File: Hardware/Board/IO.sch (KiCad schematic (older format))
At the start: 45 parts, among them U3 TJA1029T, U4 TJA1029T, U5 TJA1029T, U6 TJA1049T-3, U7 MAX3072E

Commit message: Board to Board Verbindung eingefügt
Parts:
- added C64: 100nF, Capacitor_SMD:C_0603_1608Metric, symbol Device:C
- added U2: PCF8574A, symbol Interface_Expansion:PCF8574A
- gave numbers to parts that had none: 4
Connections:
- wire segments 158 -> 178
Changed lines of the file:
@@
 EESchema Schematic File Version 4
 LIBS:Womo-cache
-EELAYER 29 0
+EELAYER 26 0
 EELAYER END
 $Descr A3 16535 11693
@@
 I2C2_SCL
 $Comp
-L Interface_Expansion:PCF8574A U?
+L Interface_Expansion:PCF8574A U1
 U 1 1 5CF888F7
 P 7200 6600
-F 0 "U?" H 6750 7350 50  0000 C CNN
+F 0 "U1" H 6750 7350 50  0000 C CNN
 F 1 "PCF8574A" H 6850 7250 50  0000 C CNN
 F 2 "" H 7200 6600 50  0001 C CNN
@@
 	7700 6200 7850 6200
 $Comp
-L power:GND #PWR?
+L power:GND #PWR0126
 U 1 1 5CFC8198
 P 6350 6750
-F 0 "#PWR?" H 6350 6500 50  0001 C CNN
+F 0 "#PWR0126" H 6350 6500 50  0001 C CNN
 F 1 "GND" H 6355 6577 50  0000 C CNN
 F 2 "" H 6350 6750 50  0001 C CNN
@@
 	6350 6700 6350 6750
 $Comp
-L power:+3.3V #PWR?
+L power:+3.3V #PWR0134
 U 1 1 5CFDD90C
 P 7200 5650
-F 0 "#PWR?" H 7200 5500 50  0001 C CNN
+F 0 "#PWR0134" H 7200 5500 50  0001 C CNN
 F 1 "+3.3V" H 7215 5823 50  0000 C CNN
 F 2 "" H 7200 5650 50  0001 C CNN
@@
 $EndComp
 $Comp
-L Device:C C?
+L Device:C C14
 U 1 1 5CFE3BF0
 P 7450 5750
-F 0 "C?" V 7198 5750 50  0000 C CNN
+F 0 "C14" V 7198 5750 50  0000 C CNN
 F 1 "100nF" V 7289 5750 50  0000 C CNN
 F 2 "Capacitor_SMD:C_0603_1608Metric" H 7488 5600 50  0001 C CNN
@@
 $EndComp
 $Comp
-L power:GND #PWR?
+L power:GND #PWR0140
 U 1 1 5CFE91D8
 P 7900 5800
-F 0 "#PWR?" H 7900 5550 50  0001 C CNN
+F 0 "#PWR0140" H 7900 5550 50  0001 C CNN
 F 1 "GND" H 7905 5627 50  0000 C CNN
 F 2 "" H 7900 5800 50  0001 C CNN
@@
 	7600 5750 7900 5750
 $Comp
-L Device:R R?
+L Device:R R49
 U 1 1 5D005AC4
 P 6150 5900
-F 0 "R?" H 6220 5946 50  0000 L CNN
+F 0 "R49" H 6220 5946 50  0000 L CNN
 F 1 "10K" H 6220 5855 50  0000 L CNN
 F 2 "Resistor_SMD:R_0603_1608Metric" V 6080 5900 50  0001 C CNN
@@
 $EndComp
 $Comp
-L power:+3.3V #PWR?
+L power:+3.3V #PWR0141
 U 1 1 5D005ACA
 P 6150 5650
-F 0 "#PWR?" H 6150 5500 50  0001 C CNN
+F 0 "#PWR0141" H 6150 5500 50  0001 C CNN
 F 1 "+3.3V" H 6165 5823 50  0000 C CNN
 F 2 "" H 6150 5650 50  0001 C CNN
@@
 	6150 5750 6150 5650
 $Comp
-L Device:R R?
+L Device:R R48
 U 1 1 5D00C9F0
 P 5850 5900
-F 0 "R?" H 5920 5946 50  0000 L CNN
+F 0 "R48" H 5920 5946 50  0000 L CNN
 F 1 "10K" H 5920 5855 50  0000 L CNN
 F 2 "Resistor_SMD:R_0603_1608Metric" V 5780 5900 50  0001 C CNN
@@
 $EndComp
 $Comp
-L power:+3.3V #PWR?
+L power:+3.3V #PWR0142
 U 1 1 5D00C9F6
 P 5850 5650
-F 0 "#PWR?" H 5850 5500 50  0001 C CNN
+F 0 "#PWR0142" H 5850 5500 50  0001 C CNN
 F 1 "+3.3V" H 5865 5823 50  0000 C CNN
 F 2 "" H 5850 5650 50  0001 C CNN
@@
 Wire Wire Line
 	6450 5750 7200 5750
+$Comp
+L power:GND #PWR0143
+U 1 1 5D029893
+P 7200 9850
+F 0 "#PWR0143" H 7200 9600 50  0001 C CNN
+F 1 "GND" H 7205 9677 50  0000 C CNN
+F 2 "" H 7200 9850 50  0001 C CNN
+F 3 "" H 7200 9850 50  0001 C CNN
+	1    7200 9850
+	1    0    0    -1
+$EndComp
+$Comp
+L Interface_Expansion:PCF8574A U2
+U 1 1 5D029899
+P 7200 9050
+F 0 "U2" H 6750 9800 50  0000 C CNN
+F 1 "PCF8574A" H 6850 9700 50  0000 C CNN
+F 2 "" H 7200 9050 50  0001 C CNN
+F 3 "http://www.nxp.com/documents/data_sheet/PCF8574_PCF8574A.pdf" H 7200 9050 50  0001 C CNN
+	1    7200 9050
+	1    0    0    -1
+$EndComp
+Text GLabel 7850 8650 2    50   Output ~ 0
+SLP-LIN1
+Text GLabel 7850 8750 2    50   Output ~ 0
+SLP-LIN2
+Text GLabel 7850 8850 2    50   Output ~ 0
+SLP-LIN3
+Text GLabel 7850 8950 2    50   Output ~ 0
+STB-CAN
+Wire Wire Line
+	7700 8950 7850 8950
+Wire Wire Line
+	7700 8850 7850 8850
+Wire Wire Line
+	7700 8750 7850 8750
+Wire Wire Line
+	7700 8650 7850 8650
+$Comp
+L power:+3.3V #PWR0144
+U 1 1 5D0298A8
+P 7200 8100
+F 0 "#PWR0144" H 7200 7950 50  0001 C CNN
+F 1 "+3.3V" H 7215 8273 50  0000 C CNN
+F 2 "" H 7200 8100 50  0001 C CNN
+F 3 "" H 7200 8100 50  0001 C CNN
+	1    7200 8100
+	1    0    0    -1
+$EndComp
+$Comp
+L Device:C C64
+U 1 1 5D0298AE
+P 7450 8200
+F 0 "C64" V 7198 8200 50  0000 C CNN
+F 1 "100nF" V 7289 8200 50  0000 C CNN
+F 2 "Capacitor_SMD:C_0603_1608Metric" H 7488 8050 50  0001 C CNN
+F 3 "~" H 7450 8200 50  0001 C CNN
+	1    7450 8200
+	0    1    1    0
+$EndComp
+$Comp
+L power:GND #PWR0146
+U 1 1 5D0298B5
+P 7900 8250
+F 0 "#PWR0146" H 7900 8000 50  0001 C CNN
+F 1 "GND" H 7905 8077 50  0000 C CNN
+F 2 "" H 7900 8250 50  0001 C CNN
+F 3 "" H 7900 8250 50  0001 C CNN
+	1    7900 8250
+	1    0    0    -1
+$EndComp
+Wire Wire Line
+	7200 8100 7200 8200
+Wire Wire Line
+	7300 8200 7200 8200
+Connection ~ 7200 8200
+Wire Wire Line
+	7200 8200 7200 8350
+Wire Wire Line
+	7900 8200 7900 8250
+Wire Wire Line
+	7600 8200 7900 8200
+Wire Wire Line
+	5850 8650 6700 8650
+Wire Wire Line
+	6150 8750 6700 8750
+Wire Wire Line
+	7200 9750 7200 9850
+Text GLabel 7850 9350 2    50   Output ~ 0
+VSW_Disp_EN
+Text GLabel 7850 9250 2    50   Output ~ 0
+5V_Raspi_EN
+Text GLabel 7850 9150 2    50   Output ~ 0
+3VA_EN
+Text GLabel 7850 9050 2    50   Output ~ 0
+5V_EN
+Wire Wire Line
+	7850 9050 7700 9050
+Wire Wire Line
+	7850 9150 7700 9150
+Wire Wire Line
+	7850 9250 7700 9250
+Wire Wire Line
+	7850 9350 7700 9350
+Wire Wire Line
+	6350 9050 6700 9050
+Wire Wire Line
+	6350 9150 6700 9150
+Wire Wire Line
+	6700 8950 6450 8950
+Wire Wire Line
+	6450 8200 7200 8200
+Text GLabel 5850 8750 0    50   BiDi ~ 0
+I2C2_SDA
+Text GLabel 5850 8650 0    50   Input ~ 0
+I2C2_SCL
 $EndSCHEMATC

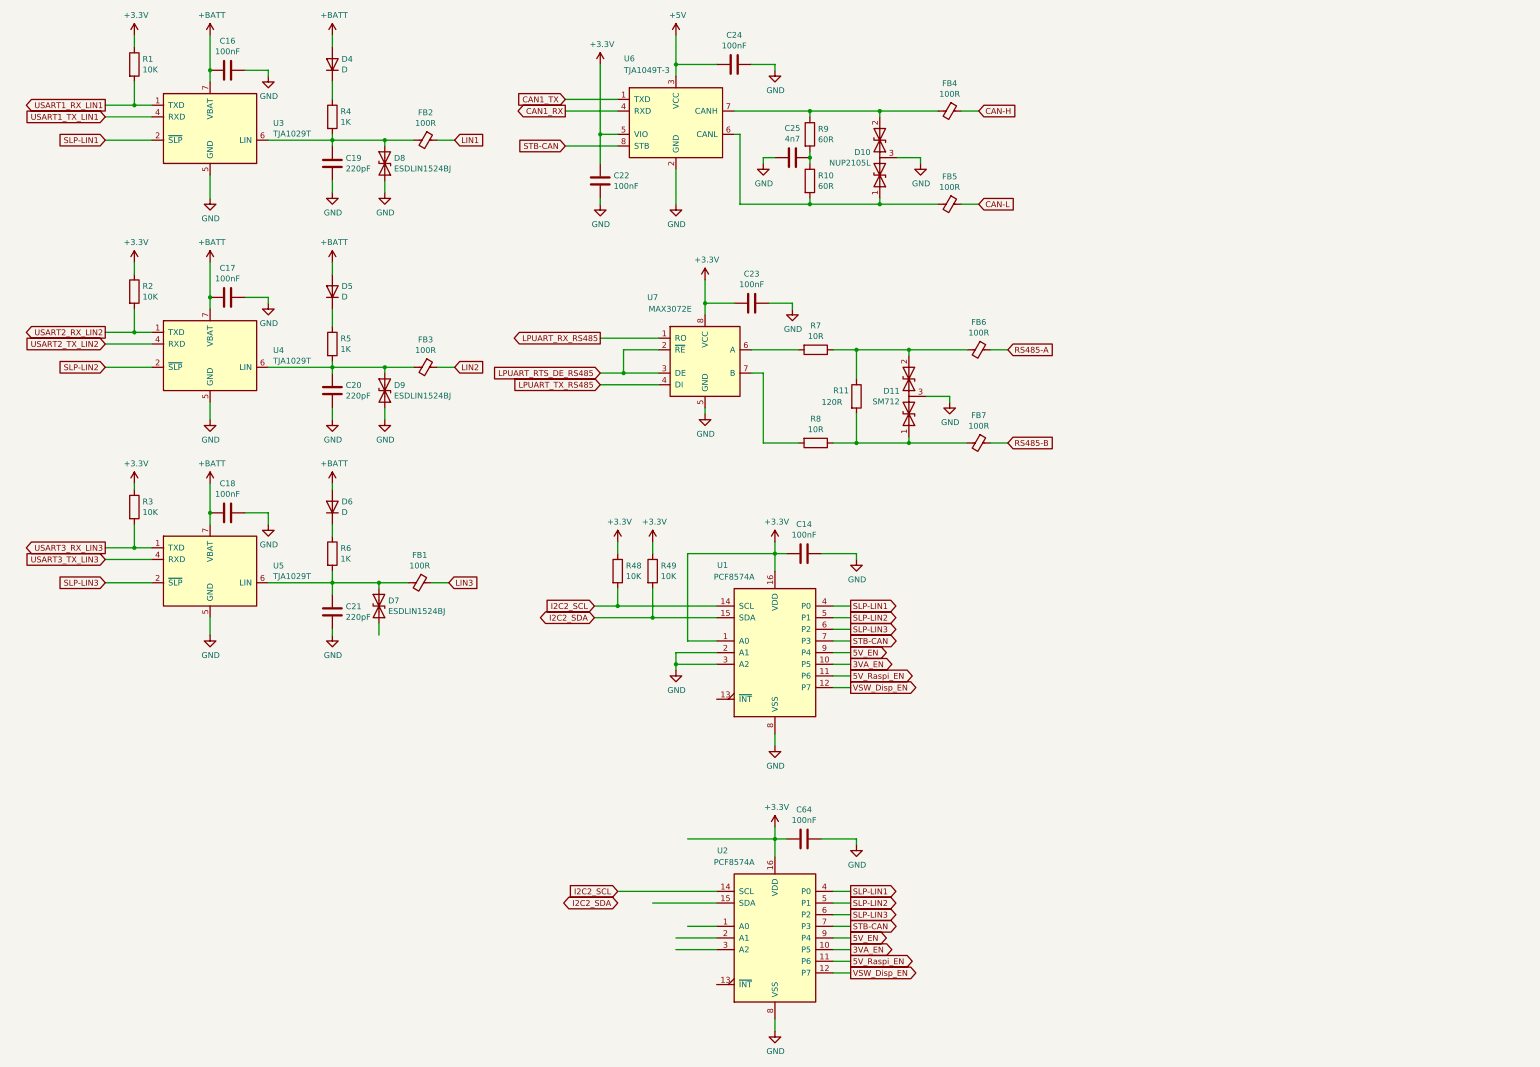
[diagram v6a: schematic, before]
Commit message: Resitiven Touch Controller eingefügt, diverse I2C Parts hinzu gefügt, Netze umgenannt
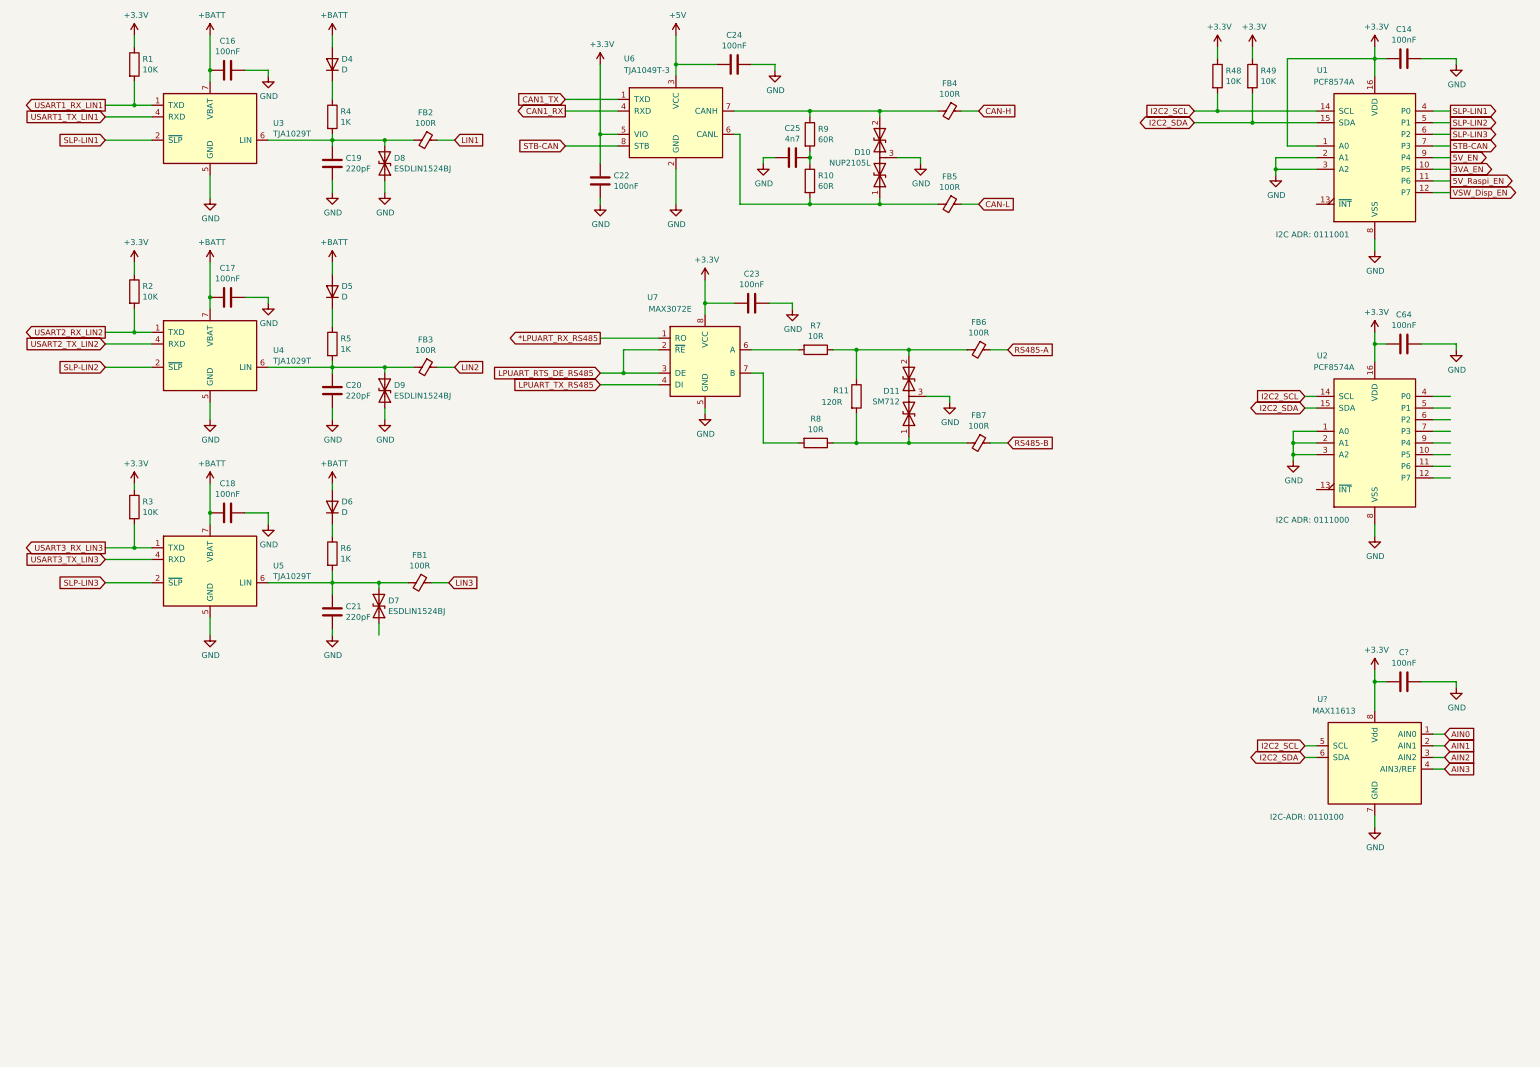
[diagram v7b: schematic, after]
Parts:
- added C?: 100nF, Capacitor_SMD:C_0603_1608Metric, symbol Device:C
- added U?: MAX11613, Package_SO:MSOP-8_3x3mm_P0.65mm, symbol Analog_ADC:MAX11613
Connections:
- net labels added: *LPUART_RX_RS485, AIN0, AIN1, AIN2, AIN3
- net labels removed: LPUART_RX_RS485
- wire segments 178 -> 192
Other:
- note added: "I2C ADR: 0111000"
- note added: "I2C ADR: 0111001"
- note added: "I2C-ADR: 0110100"
- moved on the sheet: C14, C64, R48, R49, U1, U2

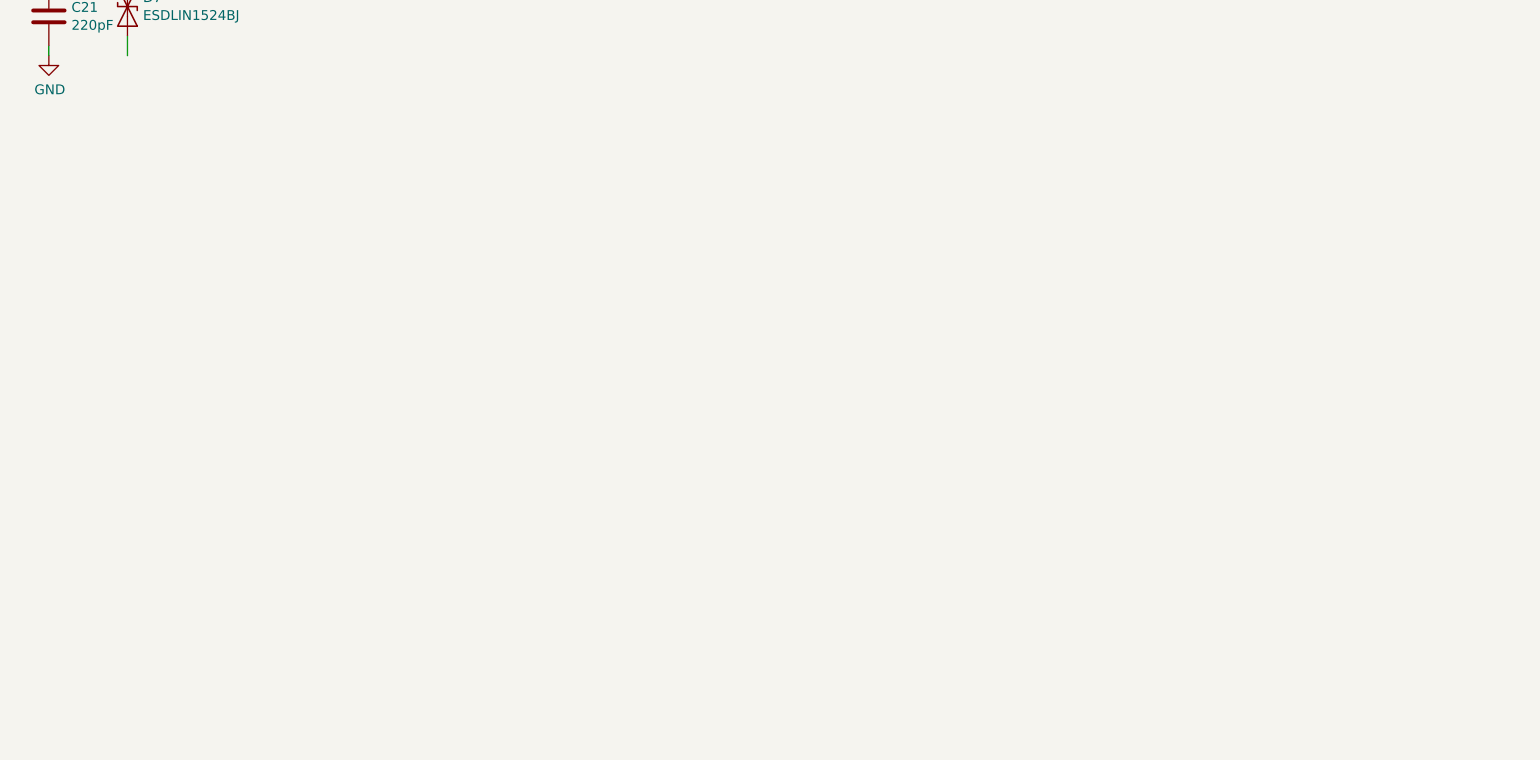
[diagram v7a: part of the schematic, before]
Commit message: GSM Modul SIM800L eingefügt, Spannung MCU Board umgenannt
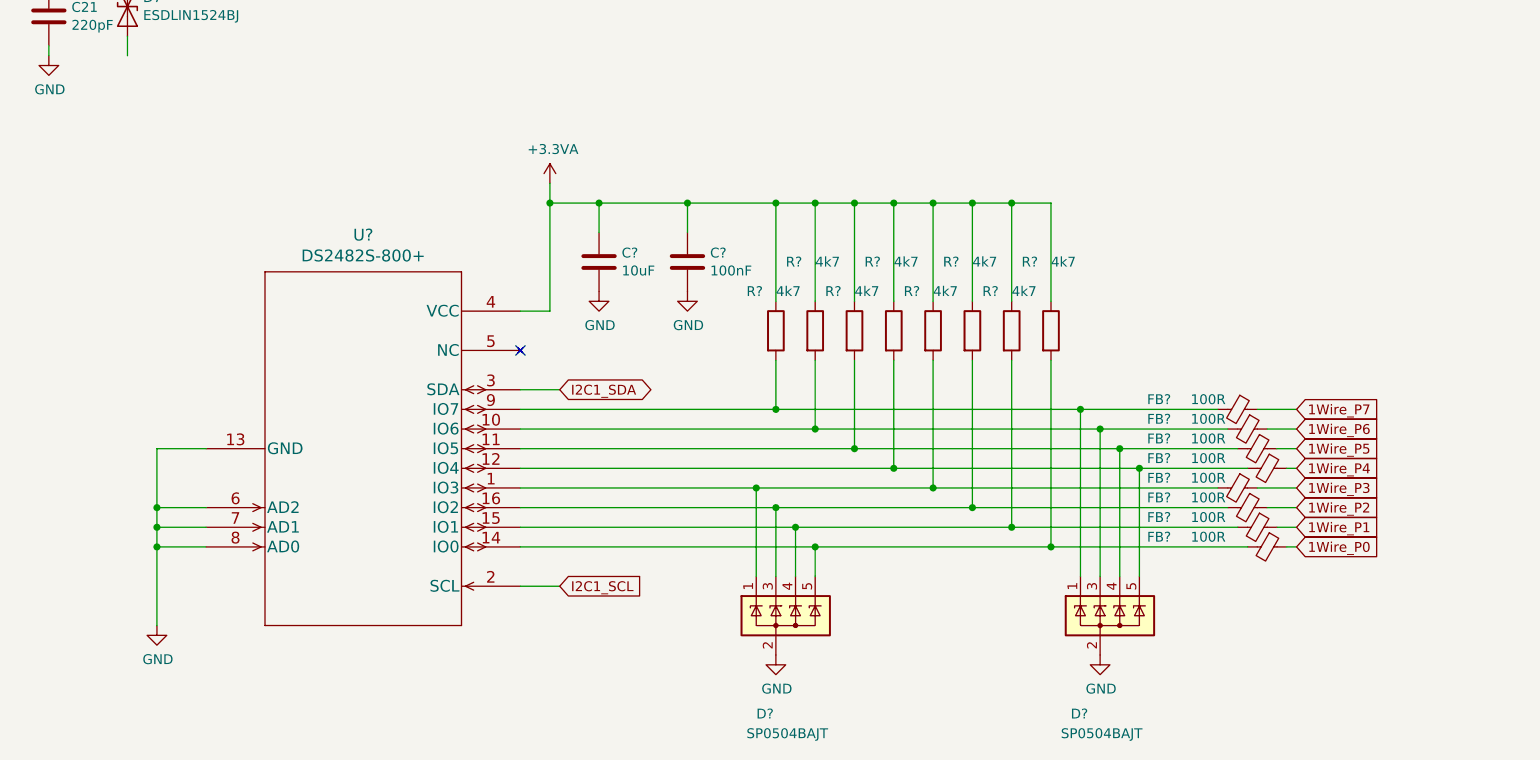
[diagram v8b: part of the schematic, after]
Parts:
- added C?: 10uF, Capacitor_SMD:C_1210_3225Metric, symbol Device:C
- added C?: 100nF, Capacitor_SMD:C_0603_1608Metric, symbol Device:C
- added D? (x2): SP0504BAJT, Package_TO_SOT_SMD:SOT-353_SC-70-5, symbol Power_Protection:SP0504BAJT
- added FB? (x8): 100R, Inductor_SMD:L_0603_1608Metric, symbol Device:Ferrite_Bead_Small
- added R? (x8): 4k7, Resistor_SMD:R_0603_1608Metric, symbol Device:R
- added U?: DS2482S-800+, Package_SO:SOIC-16_3.9x9.9mm_P1.27mm, symbol Womo-rescue:DS2482S-800+-2019-03-28_15-45-29
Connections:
- net labels added: +3.3VA, 1Wire_P0, 1Wire_P1, 1Wire_P2, 1Wire_P3, 1Wire_P4, 1Wire_P5, 1Wire_P6, 1Wire_P7, I2C1_SCL, I2C1_SDA
- wire segments 192 -> 273
- no-connect marks 0 -> 1
